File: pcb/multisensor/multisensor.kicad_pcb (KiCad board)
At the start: 2 copper layers, 50 x 40 mm, 24 parts, among them J1 TTL_Serial, J2 mmWave_Data, J3 mmWave_Support, J4 PIR_Sensor, J5 BME680, J6 BH1750, J7 USB_B_Micro, Q1 PN2222A, Q2 PN2222A, SW1 RESET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

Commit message: add tantalum caps to VCC
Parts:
- added C3: 100uf, *Multisensor:AVX-B, F.Cu at (141.2, 105.4)
- moved R6 2.19 mm to (140.7, 108.4), turned to 0 degrees
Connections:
- net GPIO12 renamed MMW_TX
- net GPIO13 renamed MMW_RX
- net GPIO14 renamed PIR
- net GPIO16 renamed MMW_IO2
- U1 pad 8: +3.3V -> Net-(U1-VCC)
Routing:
- net +3.3V: track 36.6 -> 30.4 mm
- net Net-(U1-VCC): track 0.00 -> 4.81 mm
- net GPIO0: track 42.2 -> 38.1 mm
- net PIR: track 33.4 -> 29.8 mm
- net GND: vias 15 -> 14

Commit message: update prj_img
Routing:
- net GPIO0: track 38.1 -> 43.1 mm
- net PIR: track 29.8 -> 28.7 mm
- net nRST: track 93.4 -> 92.2 mm
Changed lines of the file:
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@@
     (pad_to_mask_clearance 0)
     (aux_axis_origin 11.7 11.7)
-    (grid_origin 140.675 101.155)
+    (grid_origin 131.375 102.13)
     (pcbplotparams
       (layerselection 0x0000000_7fffffff)
-      (plot_on_all_layers_selection 0x0001020_00000000)
+      (plot_on_all_layers_selection 0x0003020_00000000)
       (disableapertmacros false)
       (usegerberextensions false)
@@
       (drillshape 2)
       (scaleselection 1)
-      (outputdirectory "../prj_img/")
+      (outputdirectory "../prj_img2/")
     )
   )
@@
     (attr smd)
     (fp_text reference "C3" (at 0.317948 -1.971302) (layer "F.SilkS")
-        (effects (font (size 0.700994 0.700994) (thickness 0.15)))
+        (effects (font (size 0.8 0.700994) (thickness 0.15)))
     )
     (fp_text value "100uF TAJB107M006RNJ" (at -0.317755 1.842993) (layer "F.Fab")
@@
     (property "ki_keywords" "connector")
     (attr through_hole)
-    (fp_text reference "J6" (at -1.83 5.05 270 unlocked) (layer "F.SilkS")
+    (fp_text reference "J6" (at -2.08 5.05 270 unlocked) (layer "F.SilkS")
         (effects (font (size 1 1) (thickness 0.15)))
     )
@@
     (property "ki_keywords" "connector")
     (attr through_hole)
-    (fp_text reference "J5" (at -2.17 6.335 90) (layer "F.SilkS")
+    (fp_text reference "J5" (at -2.18 6.225 90) (layer "F.SilkS")
         (effects (font (size 1 1) (thickness 0.15)))
     )
@@
     )
   )
-  (gr_rect (start 127.375 82.375) (end 179.375 124.375)
-    (stroke (width 0.2) (type default)) (fill none) (layer "F.Cu"))
   (gr_line (start 178.375 83.375) (end 128.375 83.375)
     (stroke (width 0.1) (type default)) (layer "Edge.Cuts"))
@@
   (segment (start 143.275 97.075) (end 145.775 97.075) (width 0.25) (layer "F.Cu") (net 14))
   (via (at 143.275 97.075) (size 0.8) (drill 0.4) (layers "F.Cu" "B.Cu") (free) (net 14))
-  (segment (start 142.2 111.455305) (end 142.2 98.15) (width 0.25) (layer "B.Cu") (net 14))
-  (segment (start 153.375 114.595) (end 150.66 111.88) (width 0.25) (layer "B.Cu") (net 14))
-  (segment (start 142.624695 111.88) (end 142.2 111.455305) (width 0.25) (layer "B.Cu") (net 14))
-  (segment (start 142.2 98.15) (end 143.275 97.075) (width 0.25) (layer "B.Cu") (net 14))
-  (segment (start 150.66 111.88) (end 142.624695 111.88) (width 0.25) (layer "B.Cu") (net 14))
+  (segment (start 144.715 113.185) (end 143.2 111.67) (width 0.25) (layer "B.Cu") (net 14))
+  (segment (start 143.2 109.854695) (end 143.475 109.579695) (width 0.25) (layer "B.Cu") (net 14))
+  (segment (start 143.475 109.579695) (end 143.475 97.275) (width 0.25) (layer "B.Cu") (net 14))
+  (segment (start 143.2 111.67) (end 143.2 109.854695) (width 0.25) (layer "B.Cu") (net 14))
+  (segment (start 143.475 97.275) (end 143.275 97.075) (width 0.25) (layer "B.Cu") (net 14))
+  (segment (start 153.375 114.595) (end 151.965 113.185) (width 0.25) (layer "B.Cu") (net 14))
+  (segment (start 151.965 113.185) (end 144.715 113.185) (width 0.25) (layer "B.Cu") (net 14))
   (segment (start 163.45038 93.075) (end 163.45038 93.075) (width 0.25) (layer "F.Cu") (net 15))
   (segment (start 176.768604 96.925) (end 177.425 97.581396) (width 0.25) (layer "F.Cu") (net 15))
@@
   (segment (start 167.475 96.411396) (end 167.988604 96.925) (width 0.25) (layer "F.Cu") (net 15))
   (via (at 163.475 93.075) (size 0.8) (drill 0.4) (layers "F.Cu" "B.Cu") (free) (net 15))
+  (segment (start 132.06 102.13) (end 139.575 94.615) (width 0.25) (layer "B.Cu") (net 15))
+  (segment (start 162.455 94.615) (end 163.475 93.595) (width 0.25) (layer "B.Cu") (net 15))
+  (segment (start 131.375 102.13) (end 132.06 102.13) (width 0.25) (layer "B.Cu") (net 15))
+  (segment (start 163.475 93.595) (end 163.475 93.075) (width 0.25) (layer "B.Cu") (net 15))
   (segment (start 139.575 94.615) (end 162.455 94.615) (width 0.25) (layer "B.Cu") (net 15))
-  (segment (start 162.455 94.615) (end 163.475 93.595) (width 0.25) (layer "B.Cu") (net 15))
-  (segment (start 163.475 93.595) (end 163.475 93.075) (width 0.25) (layer "B.Cu") (net 15))
-  (segment (start 131.375 102.13) (end 132.06 102.13) (width 0.25) (layer "B.Cu") (net 15))
-  (segment (start 132.06 102.13) (end 139.575 94.615) (width 0.25) (layer "B.Cu") (net 15))
-  (segment (start 165.58 97.375) (end 171.875 97.375) (width 0.25) (layer "F.Cu") (net 16))
   (segment (start 163.475 95.27) (end 165.58 97.375) (width 0.25) (layer "F.Cu") (net 16))
   (segment (start 173.875 99.375) (end 175.355 100.855) (width 0.25) (layer "F.Cu") (net 16))
   (segment (start 175.375 100.395) (end 175.375 100.855) (width 0.25) (layer "F.Cu") (net 16))
   (segment (start 163.475 95.075) (end 163.475 95.27) (width 0.25) (layer "F.Cu") (net 16))
+  (segment (start 165.58 97.375) (end 173.455 97.375) (width 0.25) (layer "F.Cu") (net 16))
   (segment (start 173.875 97.795) (end 173.875 99.375) (width 0.25) (layer "F.Cu") (net 16))
   (segment (start 175.355 100.855) (end 175.375 100.855) (width 0.25) (layer "F.Cu") (net 16))
   (segment (start 173.455 97.375) (end 173.875 97.795) (width 0.25) (layer "F.Cu") (net 16))
-  (segment (start 171.875 97.375) (end 172.355 97.375) (width 0.25) (layer "F.Cu") (net 16))
   (segment (start 160.975 95.075) (end 162.225 95.075) (width 0.25) (layer "F.Cu") (net 16))
   (segment (start 160.975 95.075) (end 163.475 95.075) (width 0.25) (layer "F.Cu") (net 16))
-  (segment (start 171.875 97.375) (end 173.455 97.375) (width 0.25) (layer "F.Cu") (net 16))
   (via (at 163.475 95.075) (size 0.8) (drill 0.4) (layers "F.Cu" "B.Cu") (free) (net 16))
   (segment (start 131.375 104.67) (end 132.3 104.67) (width 0.25) (layer "B.Cu") (net 16))
@@
   (segment (start 165.125 111.125) (end 171.625 111.125) (width 0.25) (layer "F.Cu") (net 31))
   (via (at 143.275 89.075) (size 0.8) (drill 0.4) (layers "F.Cu" "B.Cu") (net 31))
-  (segment (start 140.785 111.835) (end 142.1 113.15) (width 0.25) (layer "B.Cu") (net 31))
+  (segment (start 139.388604 94.165) (end 138.058604 95.495) (width 0.25) (layer "B.Cu") (net 31))
+  (segment (start 129.755 95.495) (end 129.005 96.245) (width 0.25) (layer "B.Cu") (net 31))
+  (segment (start 143.275 89.075) (end 143.275 93.495) (width 0.25) (layer "B.Cu") (net 31))
+  (segment (start 129.005 96.245) (end 129.005 110.585) (width 0.25) (layer "B.Cu") (net 31))
   (segment (start 143.275 93.495) (end 142.605 94.165) (width 0.25) (layer "B.Cu") (net 31))
-  (segment (start 139.388604 94.165) (end 138.058604 95.495) (width 0.25) (layer "B.Cu") (net 31))
-  (segment (start 129.005 96.245) (end 129.005 110.585) (width 0.25) (layer "B.Cu") (net 31))
-  (segment (start 129.755 95.495) (end 129.005 96.245) (width 0.25) (layer "B.Cu") (net 31))
-  (segment (start 142.1 113.15) (end 142.1 115.056396) (width 0.25) (layer "B.Cu") (net 31))
+  (segment (start 138.878604 111.835) (end 143.888604 116.845) (width 0.25) (layer "B.Cu") (net 31))
+  (segment (start 130.255 111.835) (end 138.878604 111.835) (width 0.25) (layer "B.Cu") (net 31))
   (segment (start 138.058604 95.495) (end 129.755 95.495) (width 0.25) (layer "B.Cu") (net 31))
-  (segment (start 143.275 89.075) (end 143.275 93.495) (width 0.25) (layer "B.Cu") (net 31))
   (segment (start 129.005 110.585) (end 130.255 111.835) (width 0.25) (layer "B.Cu") (net 31))
   (segment (start 159.405 116.845) (end 165.125 111.125) (width 0.25) (layer "B.Cu") (net 31))
-  (segment (start 130.255 111.835) (end 140.785 111.835) (width 0.25) (layer "B.Cu") (net 31))
+  (segment (start 143.888604 116.845) (end 159.405 116.845) (width 0.25) (layer "B.Cu") (net 31))
   (segment (start 142.605 94.165) (end 139.388604 94.165) (width 0.25) (layer "B.Cu") (net 31))
-  (segment (start 143.888604 116.845) (end 159.405 116.845) (width 0.25) (layer "B.Cu") (net 31))
-  (segment (start 142.1 115.056396) (end 143.888604 116.845) (width 0.25) (layer "B.Cu") (net 31))
-  (segment (start 144.850625 108.330625) (end 143.175 110.00625) (width 0.25) (layer "F.Cu") (net 32))
   (segment (start 160.975 97.075) (end 163.475 97.075) (width 0.25) (layer "F.Cu") (net 32))
   (segment (start 144.77625 108.405) (end 146.2975 106.88375) (width 0.25) (layer "F.Cu") (net 32))
+  (segment (start 144.850625 108.330625) (end 143.925 109.25625) (width 0.25) (layer "F.Cu") (net 32))
   (segment (start 141.6125 108.405) (end 144.77625 108.405) (width 0.25) (layer "F.Cu") (net 32))
-  (segment (start 143.175 110.00625) (end 143.175 110.905) (width 0.25) (layer "F.Cu") (net 32))
+  (segment (start 143.925 109.25625) (end 143.925 110.155) (width 0.25) (layer "F.Cu") (net 32))
   (via (at 163.475 97.075) (size 0.8) (drill 0.4) (layers "F.Cu" "B.Cu") (free) (net 32))
-  (via (at 143.175 110.905) (size 0.8) (drill 0.4) (layers "F.Cu" "B.Cu") (free) (net 32))
-  (segment (start 143.175 109.155) (end 143.175 110.905) (width 0.25) (layer "B.Cu") (net 32))
-  (segment (start 155.255 97.075) (end 143.175 109.155) (width 0.25) (layer "B.Cu") (net 32))
-  (segment (start 163.475 97.075) (end 155.255 97.075) (width 0.25) (layer "B.Cu") (net 32))
+  (via (at 143.925 110.155) (size 0.8) (drill 0.4) (layers "F.Cu" "B.Cu") (free) (net 32))
+  (segment (start 162.515 95.515) (end 147.485 95.515) (width 0.25) (layer "B.Cu") (net 32))
+  (segment (start 163.475 96.475) (end 162.515 95.515) (width 0.25) (layer "B.Cu") (net 32))
+  (segment (start 143.925 99.075) (end 143.925 110.155) (width 0.25) (layer "B.Cu") (net 32))
+  (segment (start 163.475 97.075) (end 163.475 96.475) (width 0.25) (layer "B.Cu") (net 32))
+  (segment (start 147.485 95.515) (end 143.925 99.075) (width 0.25) (layer "B.Cu") (net 32))
   (segment (start 145.775 103.075) (end 143.755 103.075) (width 0.25) (layer "F.Cu") (net 33))
   (segment (start 142.6355 104.1945) (end 143.755 103.075) (width 0.25) (layer "F.Cu") (net 33))

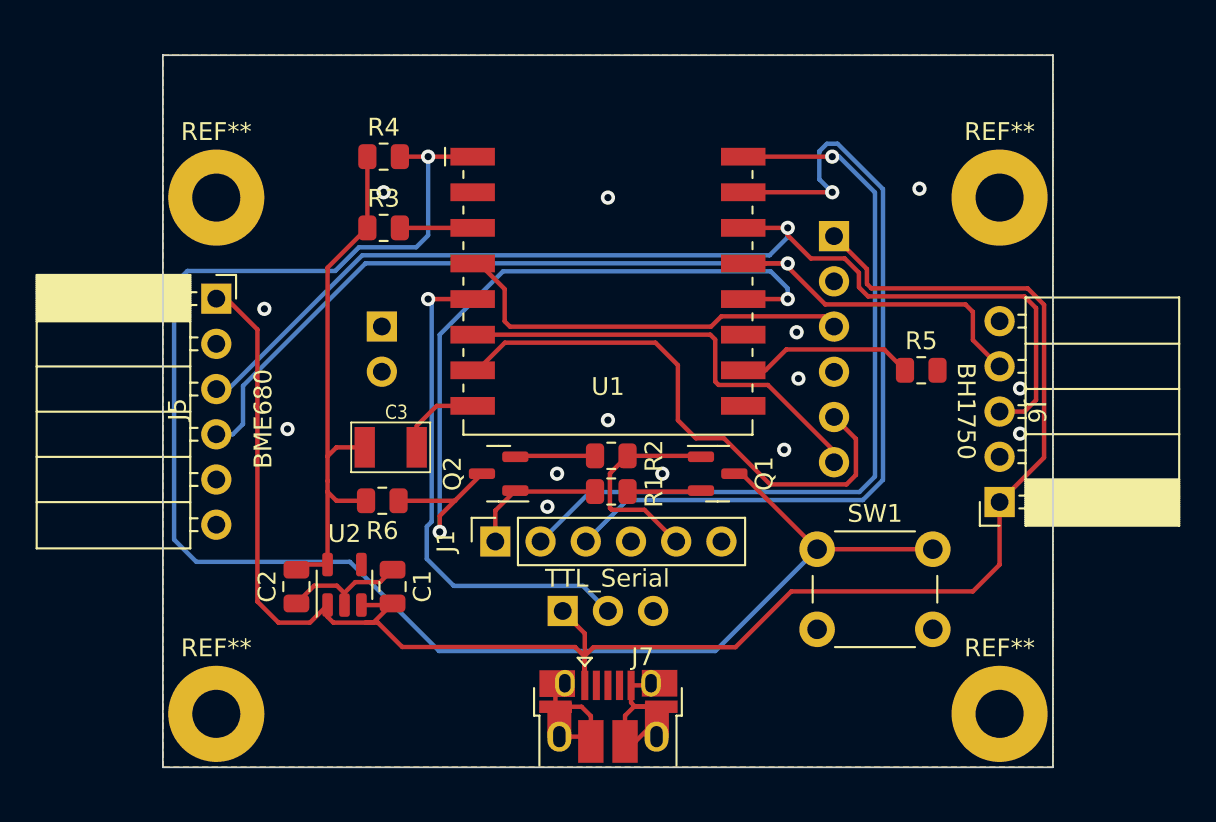
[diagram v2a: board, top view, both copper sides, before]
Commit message: add filtering caps + external pullups
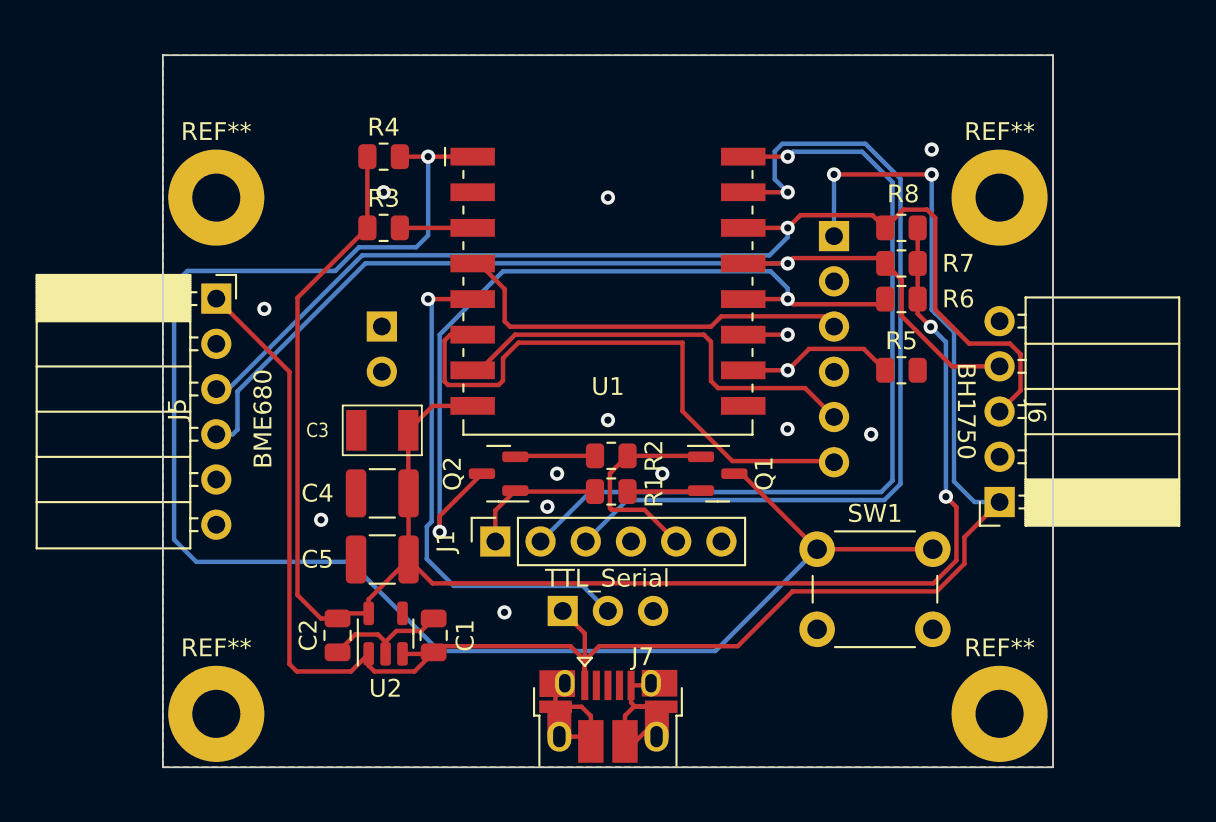
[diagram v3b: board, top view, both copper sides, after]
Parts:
- added C4: 22uF, Capacitor_SMD:C_1210_3225Metric, F.Cu at (140.7, 108.0)
- added C5: 22uF, Capacitor_SMD:C_1210_3225Metric, F.Cu at (140.7, 111.7)
- added R7: 10k, Resistor_SMD:R_0805_2012Metric, F.Cu at (169.9, 95.1)
- added R8: 10k, Resistor_SMD:R_0805_2012Metric, F.Cu at (169.9, 93.1)
- R1, R2: value 12k -> 10k
- moved R6 31.3 mm to (169.9, 97.1), turned to 180 degrees
- moved C1 3.59 mm to (143.6, 116.0)
- moved C2 3.59 mm to (138.2, 116.0)
- moved U2 3.59 mm to (140.9, 115.9)
- moved R5 1.11 mm to (169.9, 101.1)
- moved C3 1.07 mm to (140.7, 104.5), turned to 180 degrees
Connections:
- C3 pad -: Net-(U1-VCC) -> GND
- U1 pad 8: Net-(U1-VCC) -> +3.3V
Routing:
- net +3.3V: track 30.4 -> 97.8 mm, vias 0 -> 2
- net MMW_TX: track 25.0 -> 32.7 mm
- net MMW_RX: track 31.3 -> 24.3 mm
- net Net-(U1-VCC): track 4.81 -> 0.00 mm
- net +5V: track 105.8 -> 108.7 mm, vias 0 -> 2
- net TX: track 44.5 -> 47.2 mm
- net GPIO0: track 43.1 -> 45.7 mm
- net unconnected-(U1-GPIO2-Pad11): track 0.00 -> 2.50 mm, vias 0 -> 1
- net RX: track 46.9 -> 49.3 mm
- net Net-(U1-GPIO15): track 10.1 -> 8.97 mm, vias 0 -> 1
- net SDA: track 56.9 -> 56.2 mm
- net GND: vias 14 -> 12

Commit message: upadate regulator and connector
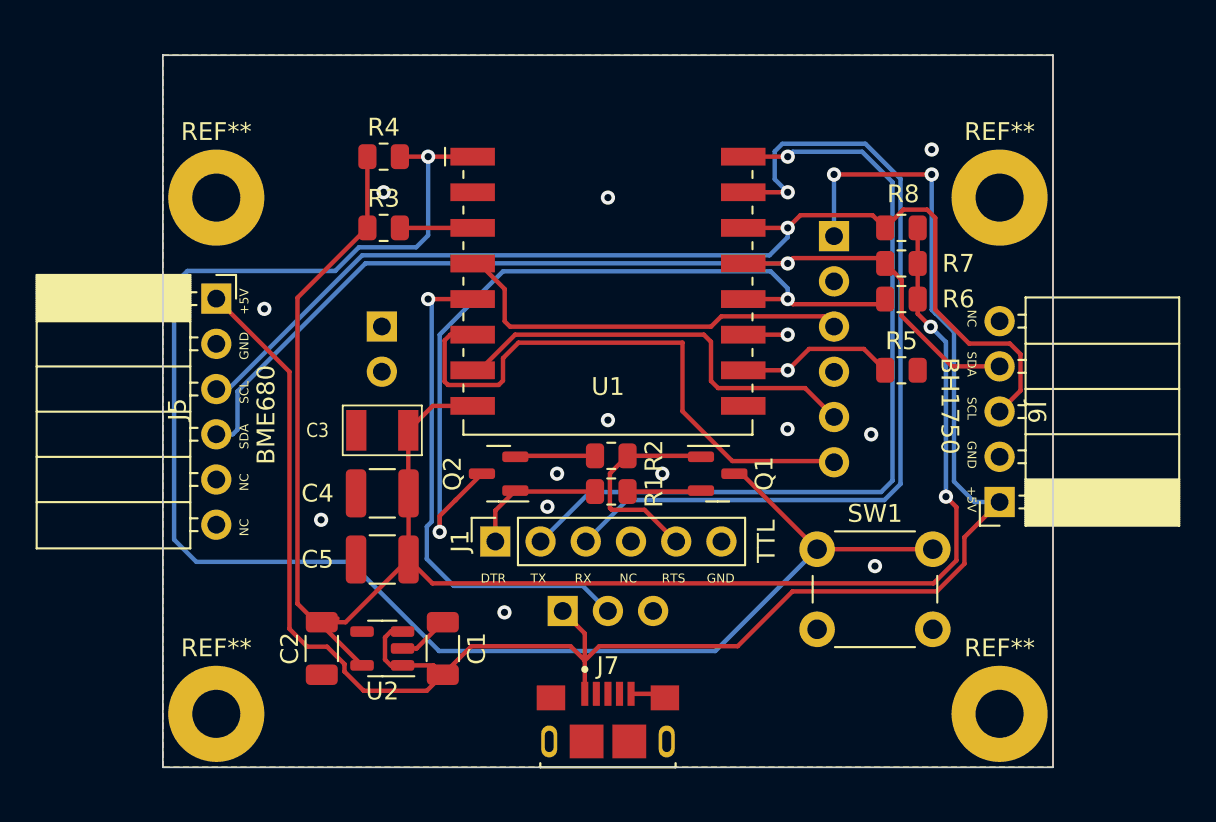
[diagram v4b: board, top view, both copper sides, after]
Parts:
- C1, C2: footprint Capacitor_SMD:C_0805_2012Metric -> Capacitor_SMD:C_1206_3216Metric
- J1: value TTL_Serial -> TTL
- J7: value USB_B_Micro -> 10118193-0001LF; footprint Connector_USB:USB_Micro-B_Amphenol_10103594-0001LF_Horizontal -> *Multisensor:AMPHENOL_10118193-0001LF
- U2: value ME6211C_SOT23-5 -> TLV75533PDBV
- moved J7 1.39 mm to (153.4, 121.9)
- moved C2 1.15 mm to (137.3, 116.7)
- moved C1 0.90 mm to (144.1, 116.7)
- moved U2 0.86 mm to (140.7, 116.7), turned to 180 degrees
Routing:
- net GND: track 26.1 -> 4.87 mm, vias 12 -> 13
- net +3.3V: track 97.8 -> 102.5 mm
- net +5V: track 108.7 -> 109.3 mm
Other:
- board text added: "+5V"
- board text added: "DTR"
- board text added: "GND"
- board text added: "NC"
- board text added: "RTS"
- board text added: "RX"
- board text added: "SCL"
- board text added: "SDA"
- board text added: "TX"

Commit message: add spice simulations and manufacturing files
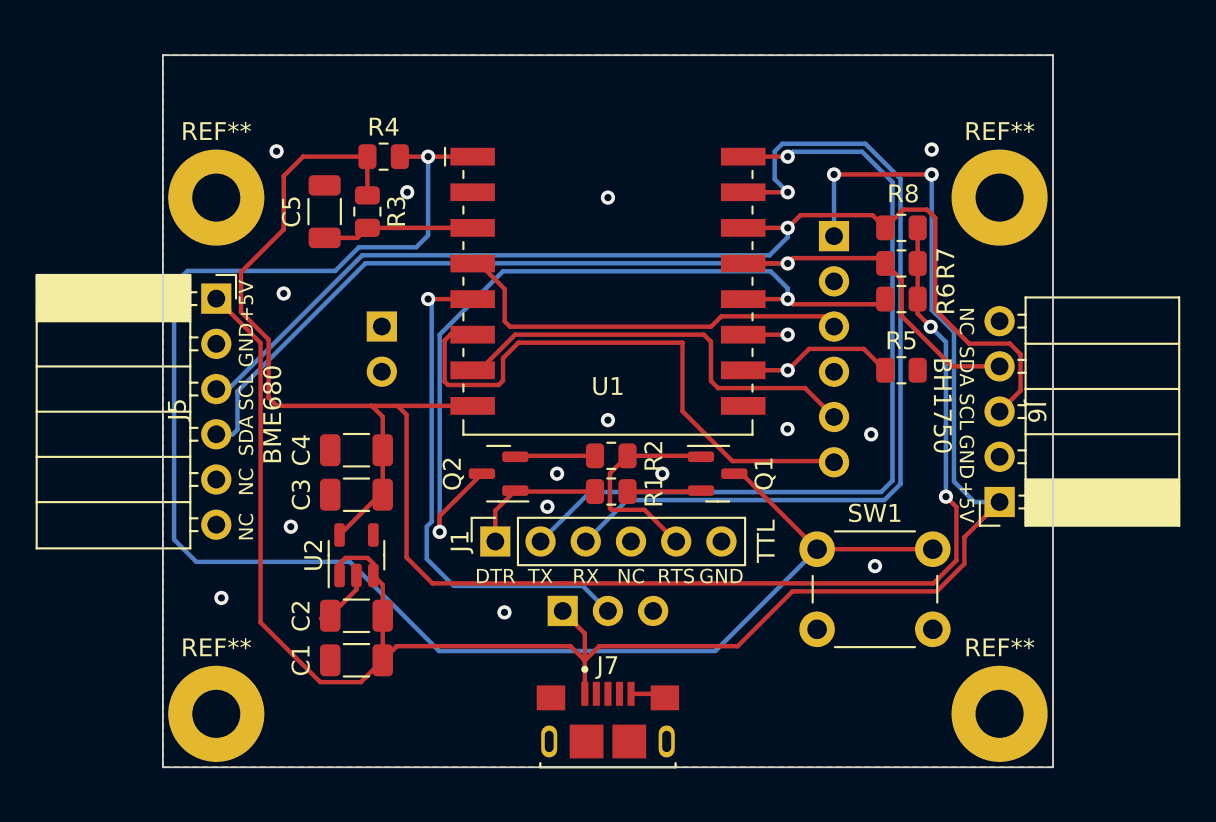
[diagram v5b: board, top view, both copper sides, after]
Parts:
- removed the C3 at (140.7, 104.5)
- added C1: 10uF, Capacitor_SMD:C_1206_3216Metric, F.Cu at (139.2, 117.4)
- C2: renamed from C1; value 1uF -> .1uF
- C3: renamed from C2; value 1uF -> 10uF
- C4: value 22uF -> .1uF; footprint Capacitor_SMD:C_1210_3225Metric -> Capacitor_SMD:C_1206_3216Metric
- C5: value 22uF -> 4.7nF; footprint Capacitor_SMD:C_1210_3225Metric -> Capacitor_SMD:C_1206_3216Metric
- moved C5 19.8 mm to (137.5, 92.2), turned to 90 degrees
- moved C3 8.85 mm to (139.2, 108.1), turned to 180 degrees
- moved U2 5.43 mm to (139.2, 111.5), turned to 90 degrees
- moved C2 5.19 mm to (139.2, 114.9), turned to 180 degrees
- moved C4 2.82 mm to (139.2, 105.6), turned to 180 degrees
- moved R3 1.29 mm to (139.9, 92.2), turned to -90 degrees
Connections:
- C4 pad 1: GND -> +3.3V
- C4 pad 2: +3.3V -> GND
- C5 pad 1: GND -> Net-(U1-EN)
- C5 pad 2: +3.3V -> GND
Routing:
- net Net-(U1-EN): track 4.09 -> 8.55 mm
- net +5V: track 109.3 -> 111.4 mm
- net GND: track 4.87 -> 5.80 mm, vias 13 -> 15
